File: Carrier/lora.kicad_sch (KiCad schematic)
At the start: 4 parts, among them J5 SMA-J-P-X-RA-TH1, U5 Ai-Thinker-Ra-01H

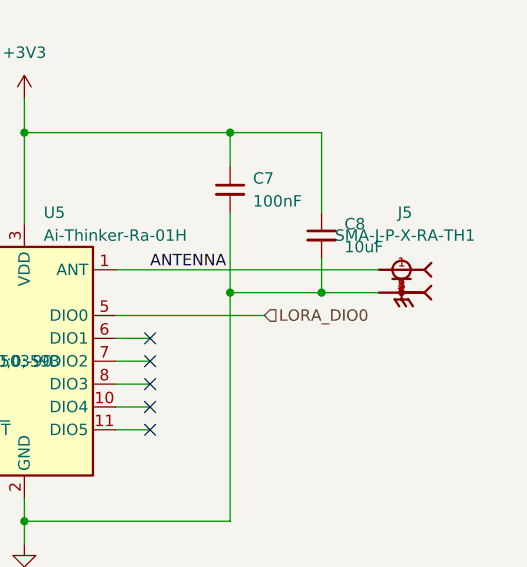
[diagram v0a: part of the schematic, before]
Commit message: fix: add ordercodes for production files
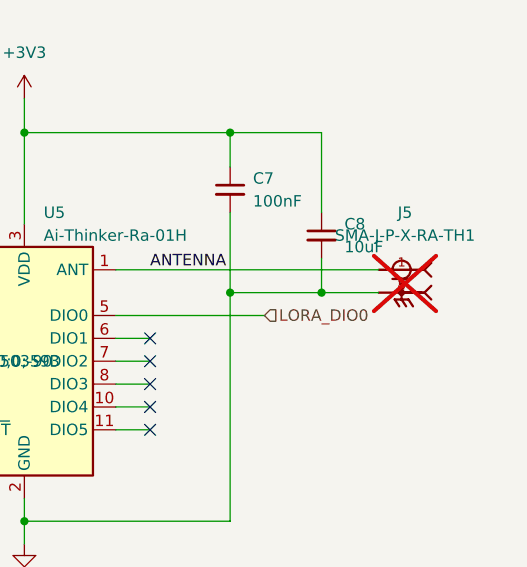
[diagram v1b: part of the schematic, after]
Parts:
- J5: now not fitted
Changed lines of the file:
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@@
 		(in_bom yes)
 		(on_board yes)
-		(dnp no)
+		(dnp yes)
 		(property "Reference" "J5"
 			(at 140.081 52.07 0)
@@
 				)
 				(justify bottom)
+				(hide yes)
+			)
+		)
+		(property "Purchase-URL" ""
+			(at 139.7 60.96 0)
+			(effects
+				(font
+					(size 1.27 1.27)
+				)
 				(hide yes)
 			)
@@
 			)
 		)
+		(property "Purchase-URL" ""
+			(at 120.65 49.53 0)
+			(effects
+				(font
+					(size 1.27 1.27)
+				)
+				(hide yes)
+			)
+		)
 		(pin "2"
 		)
@@
 			)
 		)
+		(property "Purchase-URL" ""
+			(at 97.79 68.58 0)
+			(effects
+				(font
+					(size 1.27 1.27)
+				)
+				(hide yes)
+			)
+		)
 		(pin "9"
 		)
@@
 			)
 		)
+		(property "Purchase-URL" ""
+			(at 130.81 54.61 0)
+			(effects
+				(font
+					(size 1.27 1.27)
+				)
+				(hide yes)
+			)
+		)
